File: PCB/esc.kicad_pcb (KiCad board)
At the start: 4 copper layers, 43.5 x 65 mm, 70 parts, among them J1 Conn_01x04_Pin, J2 Conn_01x01, J3 Conn_01x01, J4 Conn_01x01, J5 Conn_01x01, J6 Conn_01x01, Q1 XRS230N03C, Q2 XRS230N03C, Q3 XRS230N03C, Q4 XRS230N03C, Q5 XRS230N03C, Q6 XRS230N03C, SW1 SW_SPST, U1 STM32C031K6T6, U2 TLV76133DCY, U3 TLV9064, U4 INA180A3, U5 IRS21867S, U6 IRS21867S, U7 IRS21867S

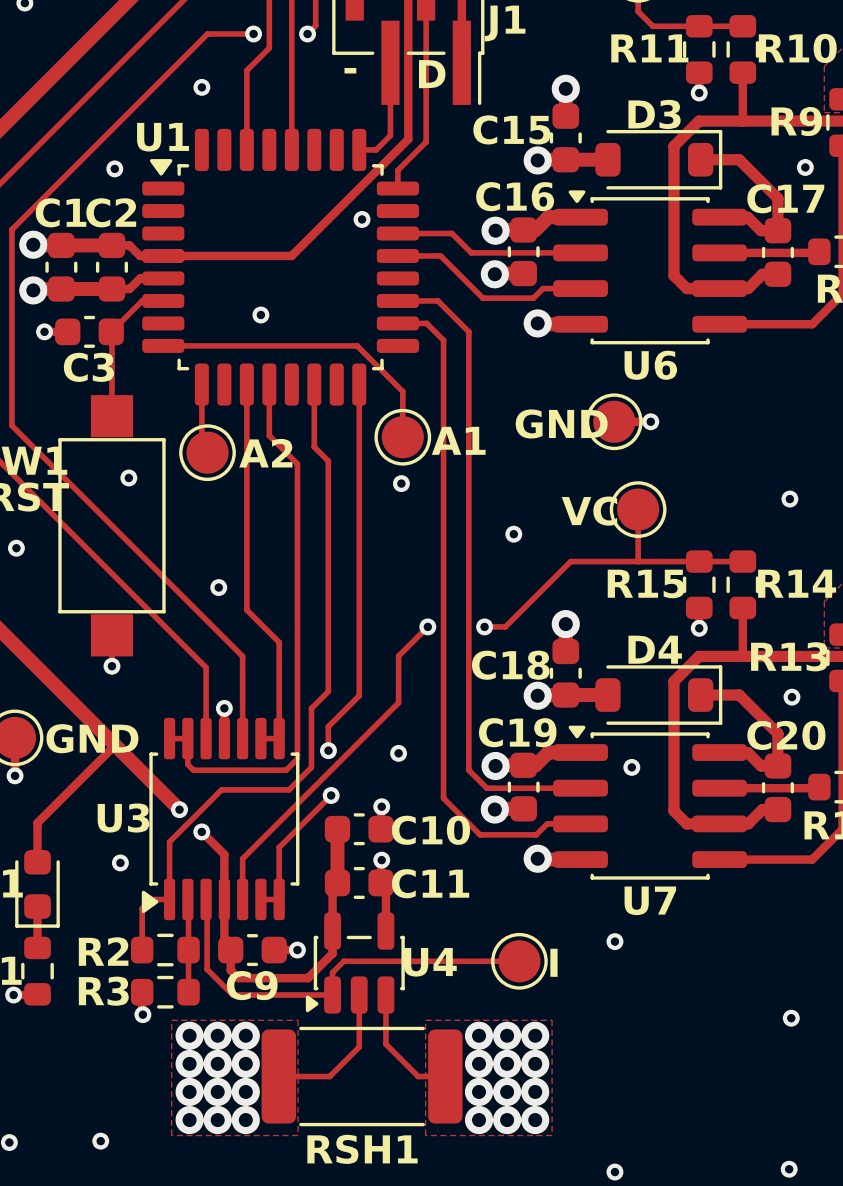
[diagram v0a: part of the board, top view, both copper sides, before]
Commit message: Added template for zero crossing detection
Done some zero crossing detection in a sample_raw.c interrupt callback.
Interrupt fires to regularly so PWM frequency had to be reduced so other
stuff could run. Currently there's a bug where the sample buffer is
always reading {0, 0, 4095, 0}.
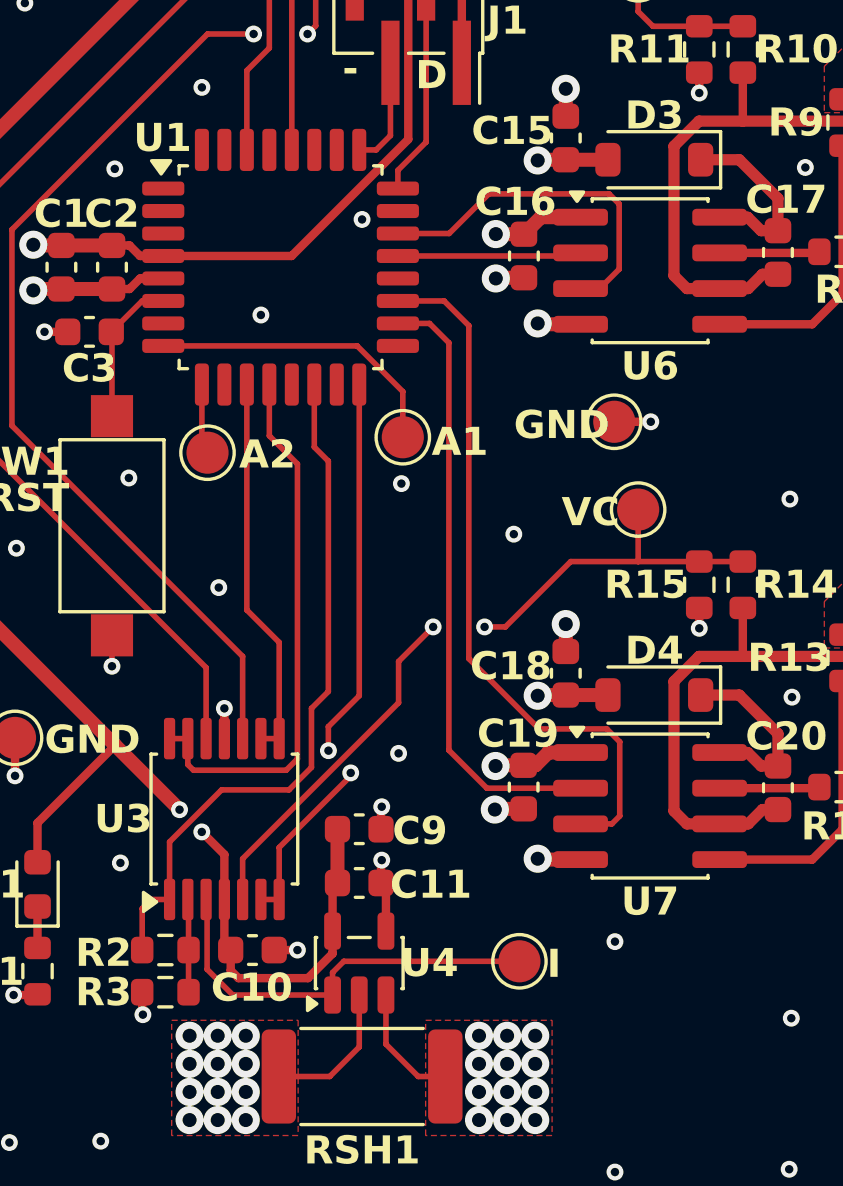
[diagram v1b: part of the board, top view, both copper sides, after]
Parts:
- moved C10 5.74 mm to (234.4, 117.6)
- moved C9 5.74 mm to (238.2, 113.3)
- moved C16 0.15 mm to (244.1, 92.9)
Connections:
- U1 pad 18: /ctrl_c_l -> /ctrl_c_h
- U1 pad 19: /ctrl_c_h -> /ctrl_c_l
- U1 pad 21: /ctrl_b_l -> /ctrl_b_h
- U1 pad 22: /ctrl_b_h -> /ctrl_b_l
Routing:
- net /ctrl_b_l: track 7.26 -> 12.6 mm
- net /ctrl_c_l: track 23.7 -> 25.5 mm
- net /ctrl_c_h: track 22.8 -> 21.8 mm
- net /v_c_buf: track 20.4 -> 20.9 mm
- net GND: vias 76 -> 75
